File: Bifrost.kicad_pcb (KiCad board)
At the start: 4 copper layers, 68.6 x 53.3 mm, 108 parts, among them IC1 DS1085Z-10+, IC2 DS1085Z-10+, J1 OIP, J10 Barrel_Jack_Switch, J5 CalCK, U1 HMC900LP5E, U2 HMC860LP3E, U5 74AHC1G04, U6 74AHC1G04

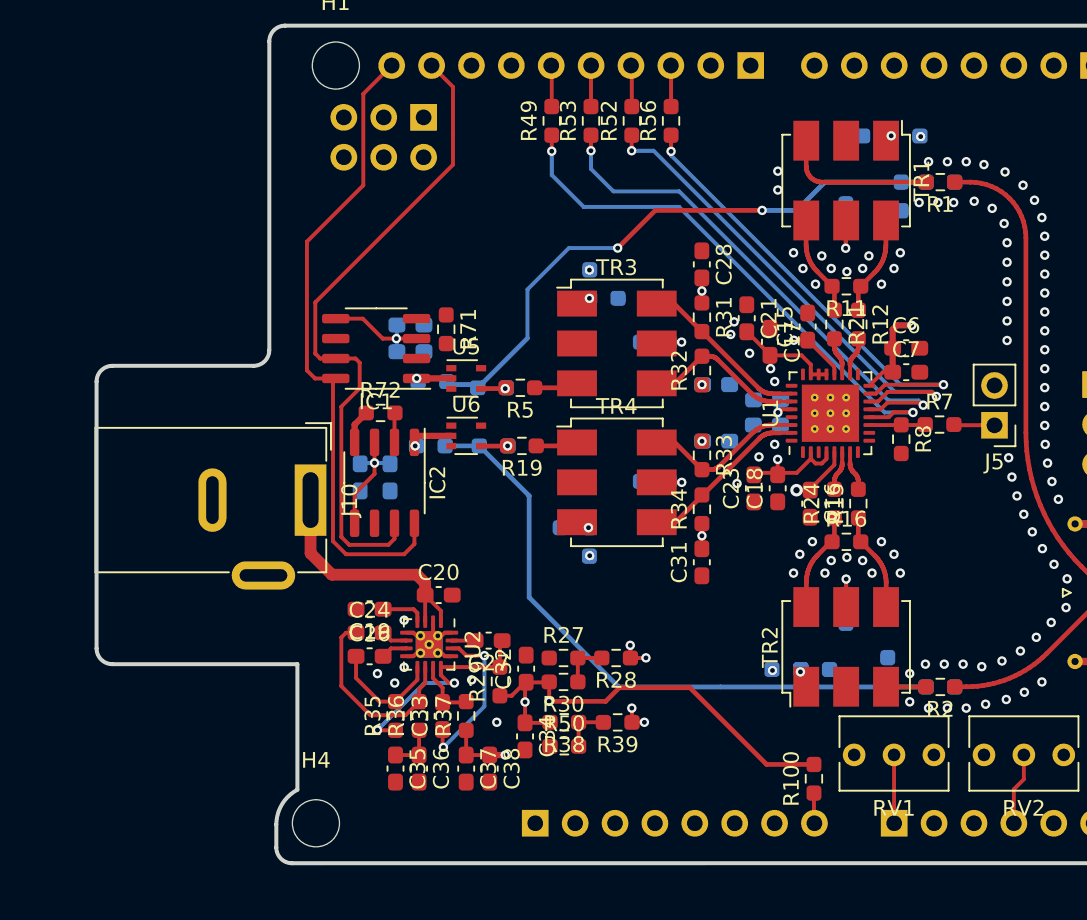
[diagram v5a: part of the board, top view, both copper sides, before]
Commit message: added cavalier on the oscillator's power
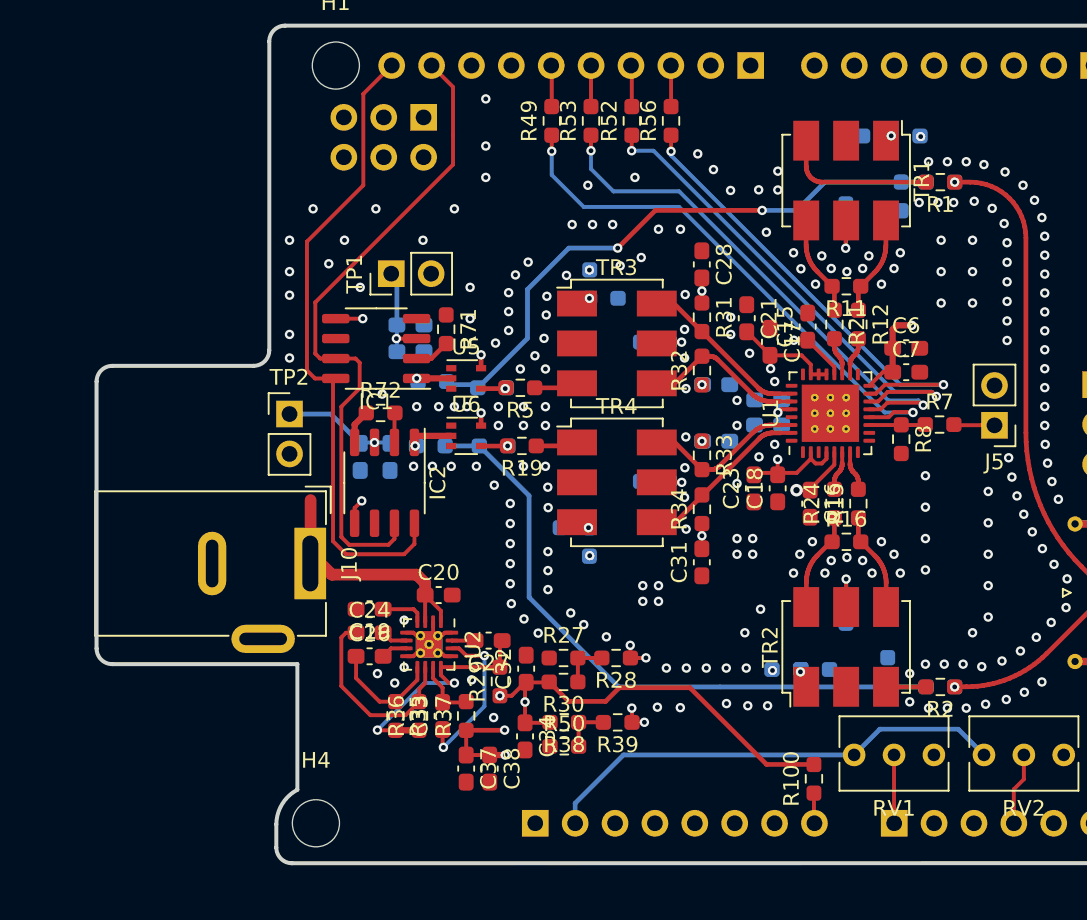
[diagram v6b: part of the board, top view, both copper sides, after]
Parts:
- removed C35: 10u, Capacitor_SMD:C_0603_1608Metric_Pad1.08x0.95mm_HandSolder
- removed C36: 100n, Capacitor_SMD:C_0603_1608Metric_Pad1.08x0.95mm_HandSolder
- added TP1: TestPoint_2Pole, Connector_PinHeader_2.54mm:PinHeader_1x02_P2.54mm_Vertical, F.Cu at (133.0, 94.1)
- added TP2: TestPoint_2Pole, Connector_PinHeader_2.54mm:PinHeader_1x02_P2.54mm_Vertical, F.Cu at (126.5, 103.1)
- R36: value 0.2 -> 1
- moved J10 4.04 mm to (114.1, 112.6)
- moved C3 1.30 mm to (132.9, 105.8)
- moved C4 1.30 mm to (131.0, 105.8)
- moved C22 0.08 mm to (157.0, 103.8)
- moved C25 0.07 mm to (157.0, 102.2)
- turned R35 to 270 degrees
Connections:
- AD1 pad 2: (no net) -> /AD1
- AD1 pad 3: (no net) -> /AD2
- AD1 pad 5: (no net) -> /AD4
- AD1 pad 6: (no net) -> /AD5
- C1 pad 2: VDDA -> Net-(C1-Pad2)
- C2 pad 2: VDDA -> Net-(C1-Pad2)
- C3 pad 2: VDDA -> Net-(C3-Pad2)
- C4 pad 2: VDDA -> Net-(C3-Pad2)
- IC1 pad 3: VDDA -> Net-(C1-Pad2)
- IC2 pad 3: VDDA -> Net-(C3-Pad2)
- ICSP1 pad 1: (no net) -> /MISO2
- ICSP1 pad 2: (no net) -> /+5V_Adr_3
- ICSP1 pad 3: (no net) -> /SCK2
- ICSP1 pad 4: (no net) -> /MOSI2
- ICSP1 pad 5: (no net) -> /RESET2
- ICSP2 pad 1: (no net) -> /MISO_0
- ICSP2 pad 3: (no net) -> /SCK_0
- ICSP2 pad 4: (no net) -> /MOSI_0
- ICSP2 pad 5: (no net) -> /RESET_0
- IOH1 pad 1: (no net) -> /IO8
- IOH1 pad 2: (no net) -> /IO9
- IOH1 pad 8: (no net) -> /AREF
- IOL1 pad 1: (no net) -> /IO0
- IOL1 pad 2: (no net) -> /IO1
- IOL1 pad 3: (no net) -> /IO2
- IOL1 pad 4: (no net) -> /IO3
- IOL1 pad 5: (no net) -> /IO4
- IOL1 pad 6: (no net) -> /IO5
- IOL1 pad 7: (no net) -> /IO6
- IOL1 pad 8: (no net) -> /IO7
- POWER1 pad 1: (no net) -> Net-(POWER1-Pad1)
- POWER1 pad 2: (no net) -> /+5V_Ard_2
- POWER1 pad 3: (no net) -> /RESET
- POWER1 pad 4: (no net) -> /+3V3
- POWER1 pad 5: (no net) -> /+5V_Ard_1
- R35 pad 1: Net-(C27-Pad1) -> Net-(C26-Pad1)
- R35 pad 2: Net-(C26-Pad1) -> Net-(C27-Pad1)
- R36 pad 1: Net-(C35-Pad1) -> Net-(C27-Pad1)
- RV1 pad 1: /+5V_Ard_0 -> /+5V_Ard_2
- RV2 pad 1: /+5V_Ard_0 -> /+5V_Ard_2
- TR1 pad 2: (no net) -> Net-(TR1-Pad2)
- TR2 pad 2: (no net) -> Net-(TR2-Pad2)
- TR3 pad 2: (no net) -> Net-(TR3-Pad2)
- TR4 pad 2: (no net) -> Net-(TR4-Pad2)
- U1 pad 1: (no net) -> Net-(U1-Pad1)
- U1 pad 10: (no net) -> Net-(U1-Pad10)
- U1 pad 17: (no net) -> Net-(U1-Pad17)
- U1 pad 24: (no net) -> Net-(U1-Pad24)
- U1 pad 25: (no net) -> Net-(U1-Pad25)
- U1 pad 29: (no net) -> Net-(U1-Pad29)
- U1 pad 3: (no net) -> Net-(U1-Pad3)
- U1 pad 32: (no net) -> Net-(U1-Pad32)
- U1 pad 8: (no net) -> Net-(U1-Pad8)
- U1 pad 9: (no net) -> Net-(U1-Pad9)
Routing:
- net /+5V_Ard_2: track 0.00 -> 29.9 mm
- net VDDA: track 60.1 -> 47.7 mm, vias 7 -> 16
- net Net-(C3-Pad2): track 0.00 -> 7.19 mm, vias 0 -> 1
- net Net-(C1-Pad2): track 0.00 -> 6.41 mm, vias 0 -> 1
- net VCC: track 59.6 -> 65.3 mm, vias 2 -> 5
- net Net-(C35-Pad1): track 3.08 -> 0.00 mm
- net Net-(IC1-Pad2): track 0.00 -> 2.28 mm
- net Net-(C27-Pad1): track 14.3 -> 15.8 mm
- net Net-(J1-Pad1): vias 0 -> 2
- net GND: vias 95 -> 208
- net CMO: vias 8 -> 10
- added copper zone on In2.Cu, net VCC

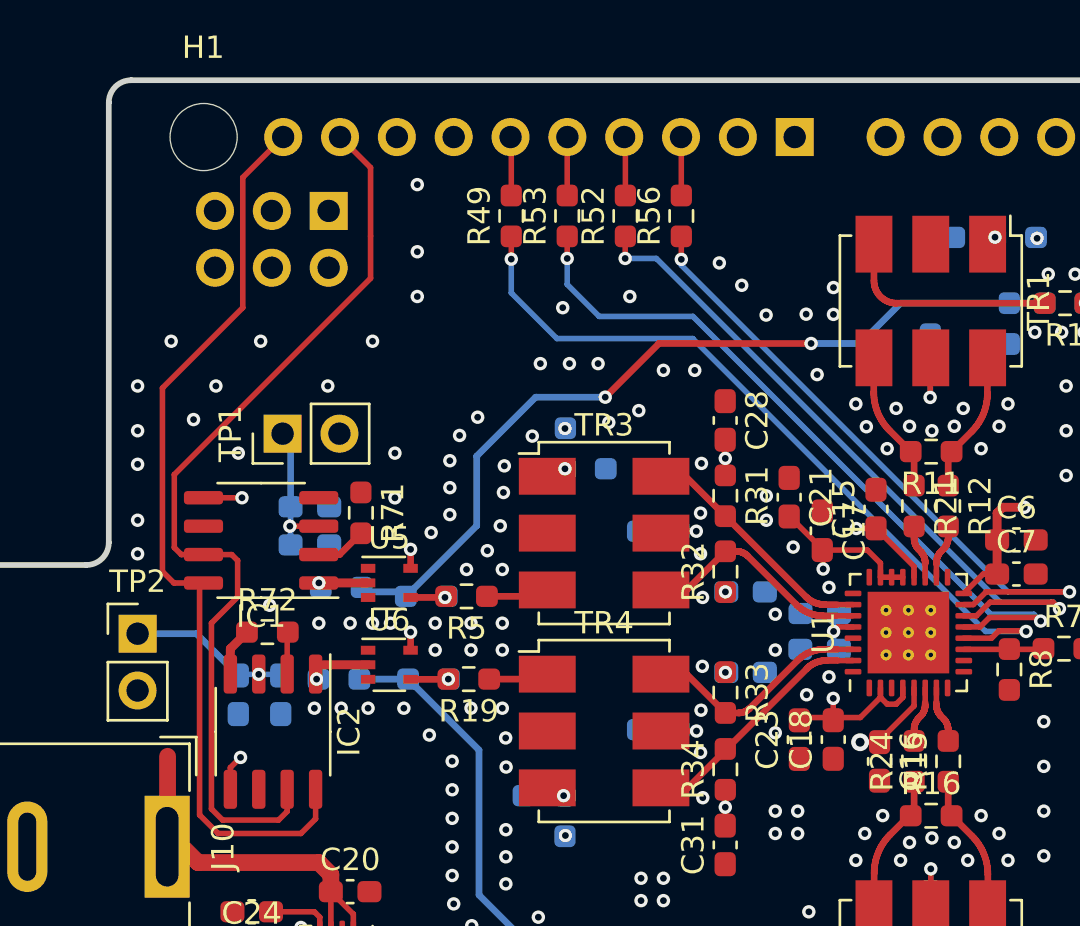
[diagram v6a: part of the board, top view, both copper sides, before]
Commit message: Connected the oscillators enable to the arduino
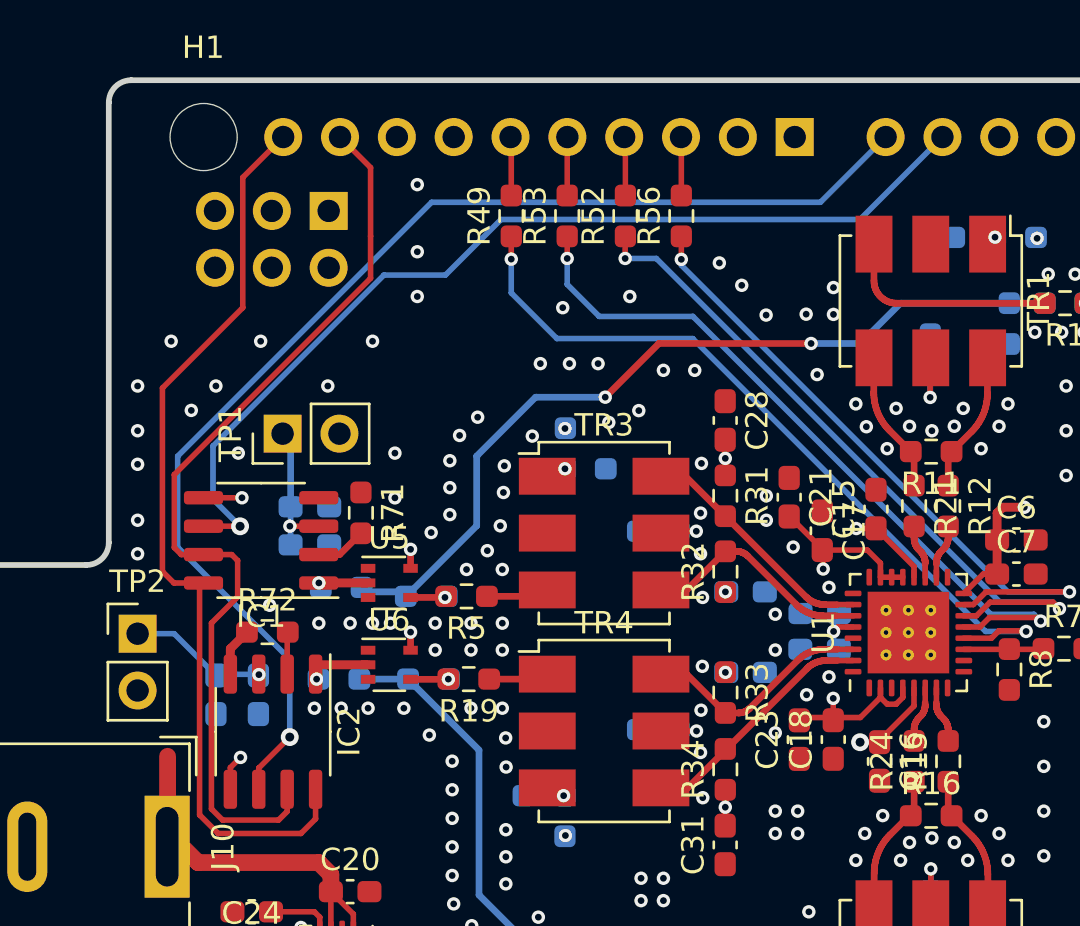
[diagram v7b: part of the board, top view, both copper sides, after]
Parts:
- moved C3 1.00 mm to (131.9, 105.8)
- moved C4 1.00 mm to (130.0, 105.8)
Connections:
- IC1 pad 6: GND -> /IO6
- IC2 pad 6: GND -> /IO7
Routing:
- net /IO7: track 0.00 -> 55.1 mm, vias 0 -> 1
- net /IO6: track 0.00 -> 44.0 mm, vias 0 -> 1
- net Net-(C3-Pad2): track 7.19 -> 6.19 mm

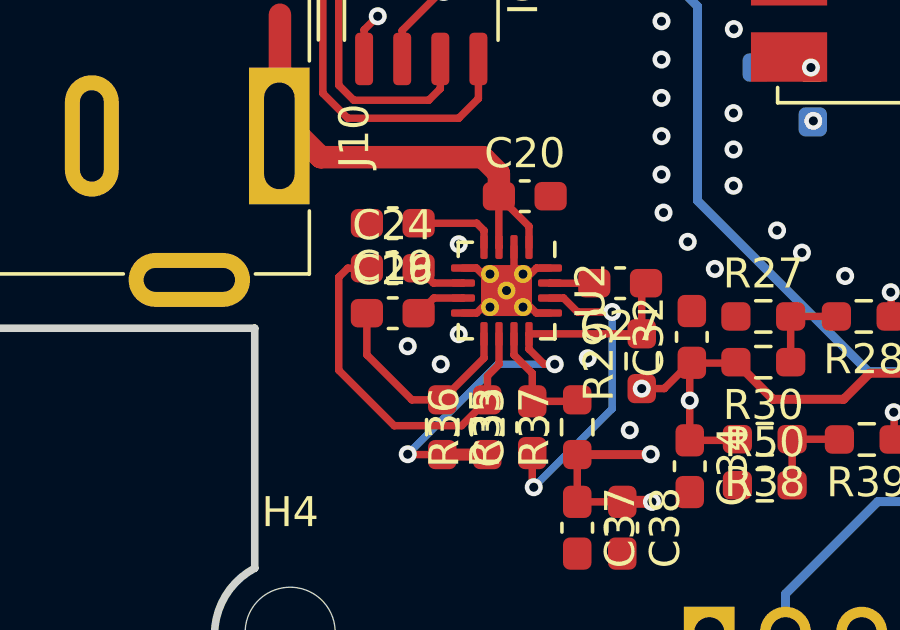
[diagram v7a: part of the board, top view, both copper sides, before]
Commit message: added the option to switch HMC860 for HMC1060
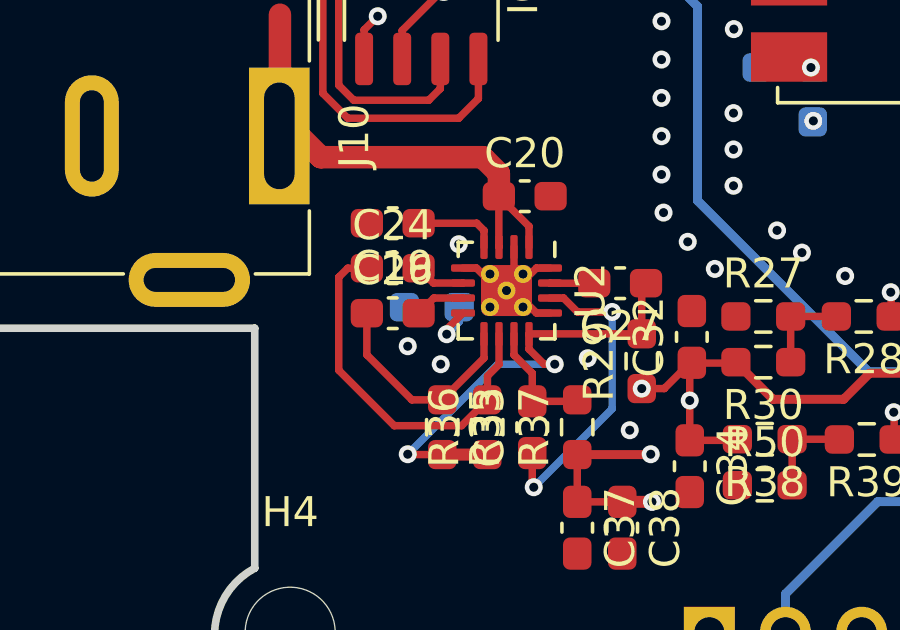
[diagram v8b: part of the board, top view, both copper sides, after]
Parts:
- added R42: 0, Resistor_SMD:R_0603_1608Metric_Pad0.98x0.95mm_HandSolder, B.Cu at (132.9, 118.3)
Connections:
- AD1 pad 2: /AD1 -> (no net)
- AD1 pad 3: /AD2 -> (no net)
- AD1 pad 5: /AD4 -> (no net)
- AD1 pad 6: /AD5 -> (no net)
- ICSP1 pad 1: /MISO2 -> (no net)
- ICSP1 pad 2: /+5V_Adr_3 -> (no net)
- ICSP1 pad 3: /SCK2 -> (no net)
- ICSP1 pad 4: /MOSI2 -> (no net)
- ICSP1 pad 5: /RESET2 -> (no net)
- ICSP2 pad 1: /MISO_0 -> (no net)
- ICSP2 pad 2: /+5V_Ard_0 -> (no net)
- ICSP2 pad 3: /SCK_0 -> (no net)
- ICSP2 pad 4: /MOSI_0 -> (no net)
- ICSP2 pad 5: /RESET_0 -> (no net)
- IOH1 pad 1: /IO8 -> (no net)
- IOH1 pad 2: /IO9 -> (no net)
- IOH1 pad 8: /AREF -> (no net)
- IOL1 pad 1: /IO0 -> (no net)
- IOL1 pad 2: /IO1 -> (no net)
- IOL1 pad 3: /IO2 -> (no net)
- IOL1 pad 4: /IO3 -> (no net)
- IOL1 pad 5: /IO4 -> (no net)
- IOL1 pad 6: /IO5 -> (no net)
- POWER1 pad 1: Net-(POWER1-Pad1) -> (no net)
- POWER1 pad 3: /RESET -> (no net)
- POWER1 pad 4: /+3V3 -> (no net)
- POWER1 pad 5: /+5V_Ard_1 -> (no net)
- TR1 pad 2: Net-(TR1-Pad2) -> (no net)
- TR2 pad 2: Net-(TR2-Pad2) -> (no net)
- TR3 pad 2: Net-(TR3-Pad2) -> (no net)
- TR4 pad 2: Net-(TR4-Pad2) -> (no net)
- U1 pad 1: Net-(U1-Pad1) -> (no net)
- U1 pad 10: Net-(U1-Pad10) -> (no net)
- U1 pad 17: Net-(U1-Pad17) -> (no net)
- U1 pad 24: Net-(U1-Pad24) -> (no net)
- U1 pad 25: Net-(U1-Pad25) -> (no net)
- U1 pad 29: Net-(U1-Pad29) -> (no net)
- U1 pad 3: Net-(U1-Pad3) -> (no net)
- U1 pad 32: Net-(U1-Pad32) -> (no net)
- U1 pad 8: Net-(U1-Pad8) -> (no net)
- U1 pad 9: Net-(U1-Pad9) -> (no net)
- U2 pad 8: GND -> Net-(R42-Pad2)
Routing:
- net Net-(R42-Pad2): track 0.00 -> 2.00 mm, vias 0 -> 1
- net GND: track 10.5 -> 8.77 mm, vias 208 -> 207
